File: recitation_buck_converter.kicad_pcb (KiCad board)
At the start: 2 copper layers, 25.4 x 25.4 mm, 11 parts, among them J1 VIN, J2 Conn_01x02_MountingPin, U1 TPS54233

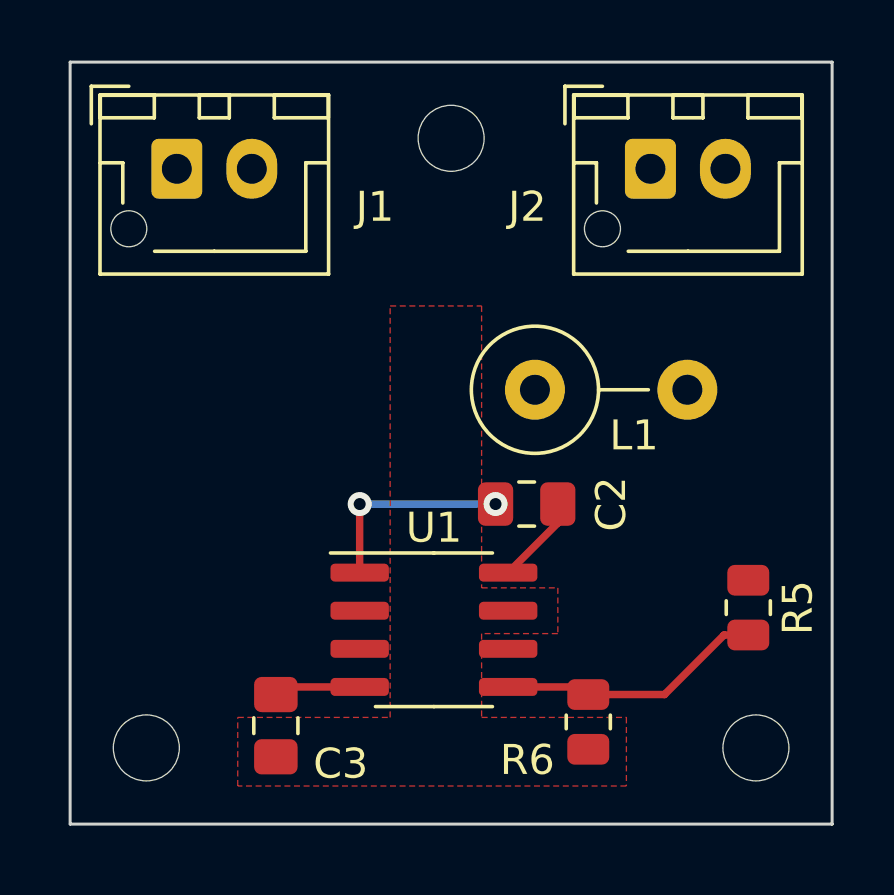
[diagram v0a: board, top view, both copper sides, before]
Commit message: feat: add output components, float EN, and layouu with good track width
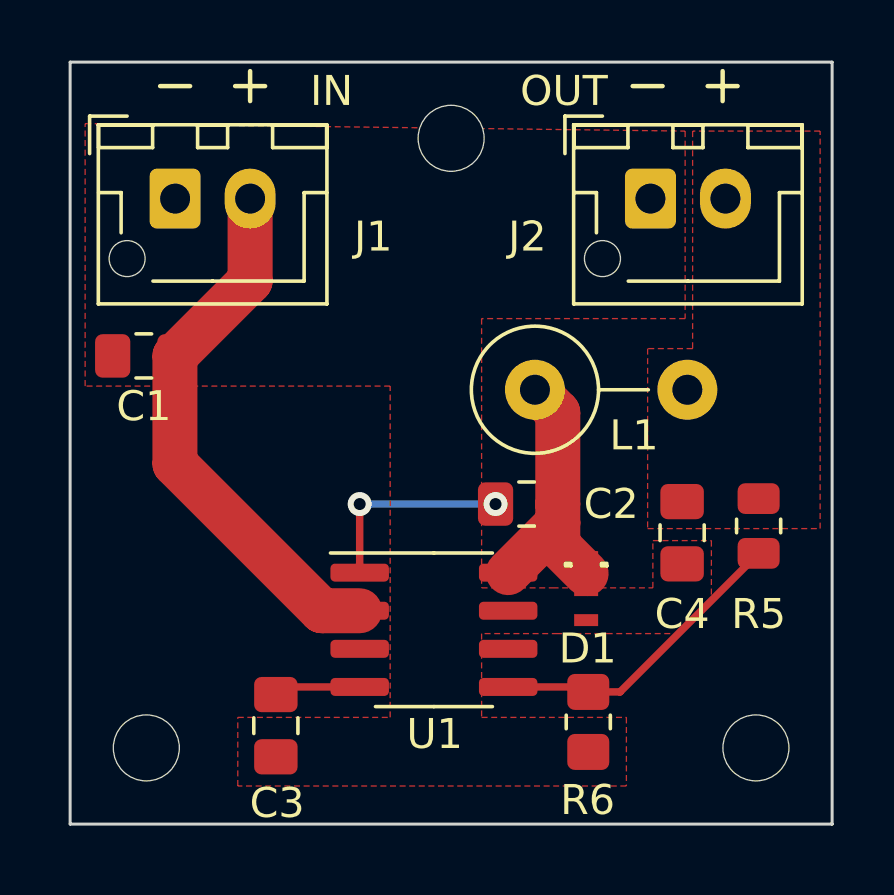
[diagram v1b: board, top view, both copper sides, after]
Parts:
- added C1: 10u, Capacitor_SMD:C_0805_2012Metric_Pad1.18x1.45mm_HandSolder, F.Cu at (129.5, 86.0)
- added C4: 1.5u, Capacitor_SMD:C_0805_2012Metric_Pad1.18x1.45mm_HandSolder, F.Cu at (147.4, 91.9)
- added D1: D_Schottky, ToshibaUS2H:US2H, F.Cu at (144.2, 94.0)
- J1: value VIN -> Conn_01x02_MountingPin
- R6: footprint Resistor_SMD:R_0805_2012Metric -> Resistor_SMD:R_0805_2012Metric_Pad1.20x1.40mm_HandSolder
- moved R5 2.74 mm to (149.9, 91.7)
- moved J1 1.00 mm to (130.5, 80.8)
- moved J2 0.99 mm to (146.3, 80.8)
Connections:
- U1 pad 3: VIN -> unconnected-(U1-EN-Pad3)
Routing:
- net VIN: track 0.00 -> 18.1 mm
- net Net-(D1-K): track 2.97 -> 9.17 mm
- net /Feedback/Vsense: track 8.93 -> 10.4 mm
- added copper zone on F.Cu, net VOUT
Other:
- board text added: "IN"
- board text added: "OUT"

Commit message: feat: add compensation network; finish pcb
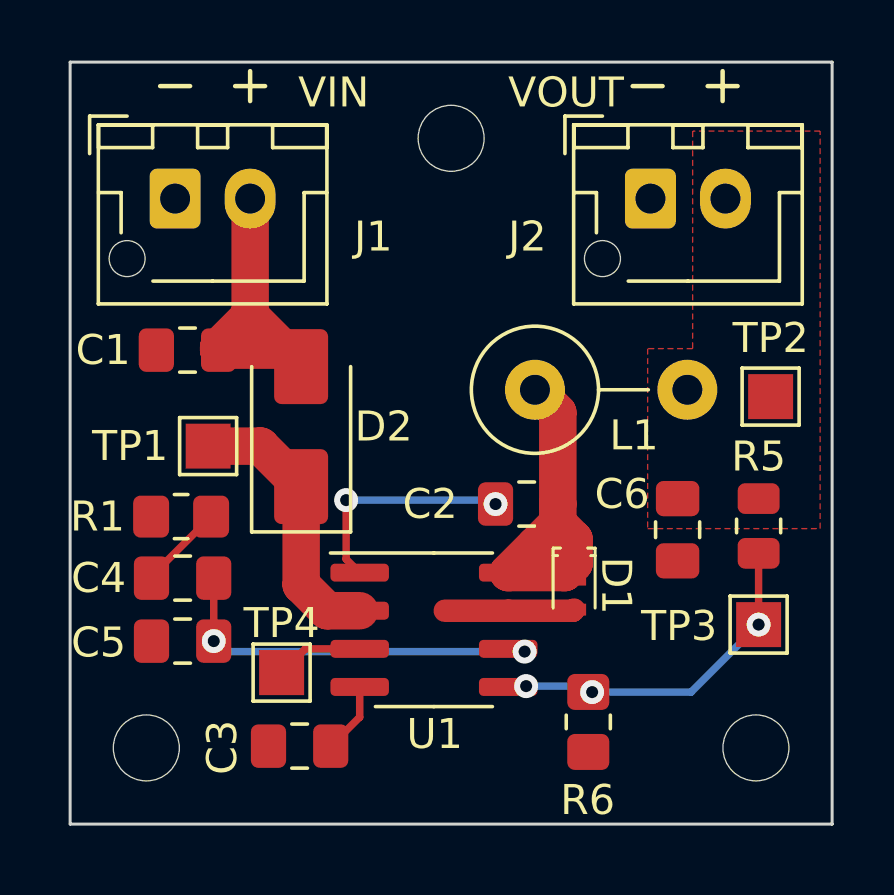
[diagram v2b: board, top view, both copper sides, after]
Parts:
- added C5: 240p, Capacitor_SMD:C_0805_2012Metric_Pad1.18x1.45mm_HandSolder, F.Cu at (130.8, 95.5)
- added C6: 1.5u, Capacitor_SMD:C_0805_2012Metric_Pad1.18x1.45mm_HandSolder, F.Cu at (147.2, 91.8)
- added D2: D, Diode_SMD:D_SMA, F.Cu at (134.7, 88.3)
- added R1: 5.23k, Resistor_SMD:R_0805_2012Metric_Pad1.20x1.40mm_HandSolder, F.Cu at (130.7, 91.3)
- added TP1: TPVin, TestPoint:TestPoint_Pad_1.5x1.5mm, F.Cu at (131.6, 89.0)
- added TP2: TPVout, TestPoint:TestPoint_Pad_1.5x1.5mm, F.Cu at (150.3, 87.3)
- added TP3: TPVsense, TestPoint:TestPoint_Pad_1.5x1.5mm, F.Cu at (149.9, 95.0)
- added TP4: TPEN, TestPoint:TestPoint_Pad_1.5x1.5mm, F.Cu at (134.1, 96.5)
- C4: value 1.5u -> 820p
- J1, J2: value Conn_01x02_MountingPin -> Conn_01x02_Pin
- moved C4 16.7 mm to (130.8, 93.4), turned to 180 degrees
- moved C1 1.47 mm to (130.9, 85.8)
- moved C3 1.04 mm to (134.7, 99.0), turned to 180 degrees
- moved D1 0.53 mm to (143.8, 93.7)
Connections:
- net Net-(D1-K) renamed PHPin
- C4 pad 1: VOUT -> Net-(U1-COMP)
- C4 pad 2: GND -> Net-(C4-Pad2)
- U1 pad 2: VIN -> Net-(D2-K)
- U1 pad 3: unconnected-(U1-EN-Pad3) -> TPS5_EN
- U1 pad 6: unconnected-(U1-COMP-Pad6) -> Net-(U1-COMP)
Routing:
- net Net-(U1-COMP): track 0.00 -> 13.2 mm, vias 0 -> 2
- net Net-(D2-K): track 0.00 -> 9.24 mm
- net VIN: track 18.1 -> 10.9 mm
- net GND: track 0.00 -> 4.33 mm
- net PHPin: track 9.17 -> 12.5 mm
- net TPS5_EN: track 0.00 -> 2.93 mm
- net Net-(C4-Pad2): track 0.00 -> 2.87 mm
- net /Feedback/Vsense: track 10.4 -> 11.9 mm, vias 0 -> 3
- net Net-(U1-BOOT): track 6.82 -> 7.64 mm
- net Net-(U1-SS): track 2.90 -> 2.37 mm
- added copper zone on B.Cu, net GND
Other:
- board text added: "VIN"
- board text added: "VOUT"
- board text removed: "IN"
- board text removed: "OUT"

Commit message: fix(pcb): move dimensions to drawing layer
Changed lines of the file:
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@@
       (outputformat 1)
       (mirror false)
-      (drillshape 1)
+      (drillshape 0)
       (scaleselection 1)
-      (outputdirectory "")
+      (outputdirectory "plot_gerbers/")
     )
   )
@@
     (fp_line (start 1 0.625) (end -1 0.625)
       (stroke (width 0.1) (type solid)) (layer "F.Fab"))
-    (pad "1" smd roundrect (at -1 0 180) (size 1.2 1.4) (layers "F.Cu" "F.Paste" "F.Mask") (roundrect_rratio 0.208333)
+    (pad "1" smd roundrect (at -1 0 180) (size 1.2 1.4) (layers "F.Cu" "F.Paste" "F.Mask") (roundrect_rratio 0.2083333333)
       (net 9 "Net-(C4-Pad2)") (pintype "passive"))
-    (pad "2" smd roundrect (at 1 0 180) (size 1.2 1.4) (layers "F.Cu" "F.Paste" "F.Mask") (roundrect_rratio 0.208333)
+    (pad "2" smd roundrect (at 1 0 180) (size 1.2 1.4) (layers "F.Cu" "F.Paste" "F.Mask") (roundrect_rratio 0.2083333333)
       (net 3 "GND") (pintype "passive"))
     (model "${KICAD6_3DMODEL_DIR}/Resistor_SMD.3dshapes/R_0805_2012Metric.wrl"
@@
     (fp_line (start 1 0.625) (end -1 0.625)
       (stroke (width 0.1) (type solid)) (layer "F.Fab"))
-    (pad "1" smd roundrect (at -1.0375 0 180) (size 1.175 1.45) (layers "F.Cu" "F.Paste" "F.Mask") (roundrect_rratio 0.212766)
+    (pad "1" smd roundrect (at -1.0375 0 180) (size 1.175 1.45) (layers "F.Cu" "F.Paste" "F.Mask") (roundrect_rratio 0.2127659574)
       (net 2 "Net-(U1-SS)") (pintype "passive"))
-    (pad "2" smd roundrect (at 1.0375 0 180) (size 1.175 1.45) (layers "F.Cu" "F.Paste" "F.Mask") (roundrect_rratio 0.212766)
+    (pad "2" smd roundrect (at 1.0375 0 180) (size 1.175 1.45) (layers "F.Cu" "F.Paste" "F.Mask") (roundrect_rratio 0.2127659574)
       (net 3 "GND") (pintype "passive"))
     (model "${KICAD6_3DMODEL_DIR}/Capacitor_SMD.3dshapes/C_0805_2012Metric.wrl"
@@
     (fp_line (start 1 0.625) (end -1 0.625)
       (stroke (width 0.1) (type solid)) (layer "F.Fab"))
-    (pad "1" smd roundrect (at -1.0375 0 180) (size 1.175 1.45) (layers "F.Cu" "F.Paste" "F.Mask") (roundrect_rratio 0.212766)
+    (pad "1" smd roundrect (at -1.0375 0 180) (size 1.175 1.45) (layers "F.Cu" "F.Paste" "F.Mask") (roundrect_rratio 0.2127659574)
       (net 4 "VIN") (pintype "passive"))
-    (pad "2" smd roundrect (at 1.0375 0 180) (size 1.175 1.45) (layers "F.Cu" "F.Paste" "F.Mask") (roundrect_rratio 0.212766)
+    (pad "2" smd roundrect (at 1.0375 0 180) (size 1.175 1.45) (layers "F.Cu" "F.Paste" "F.Mask") (roundrect_rratio 0.2127659574)
       (net 3 "GND") (pintype "passive"))
     (model "${KICAD6_3DMODEL_DIR}/Capacitor_SMD.3dshapes/C_0805_2012Metric.wrl"
@@
       (stroke (width 0.1) (type solid)) (layer "F.Fab"))
     (pad "" np_thru_hole circle (at -1.6 2) (size 1.2 1.2) (drill 1.2) (layers "*.Cu" "*.Mask"))
-    (pad "1" thru_hole roundrect (at 0 0) (size 1.7 2) (drill 1) (layers "*.Cu" "*.Mask") (roundrect_rratio 0.147059)
+    (pad "1" thru_hole roundrect (at 0 0) (size 1.7 2) (drill 1) (layers "*.Cu" "*.Mask") (roundrect_rratio 0.1470588235)
       (net 3 "GND") (pinfunction "Pin_1") (pintype "passive"))
     (pad "2" thru_hole oval (at 2.5 0) (size 1.7 2) (drill 1) (layers "*.Cu" "*.Mask")
@@
     (fp_line (start 1 0.625) (end -1 0.625)
       (stroke (width 0.1) (type solid)) (layer "F.Fab"))
-    (pad "1" smd roundrect (at -1.0375 0 270) (size 1.175 1.45) (layers "F.Cu" "F.Paste" "F.Mask") (roundrect_rratio 0.212766)
+    (pad "1" smd roundrect (at -1.0375 0 270) (size 1.175 1.45) (layers "F.Cu" "F.Paste" "F.Mask") (roundrect_rratio 0.2127659574)
       (net 5 "VOUT") (pintype "passive"))
-    (pad "2" smd roundrect (at 1.0375 0 270) (size 1.175 1.45) (layers "F.Cu" "F.Paste" "F.Mask") (roundrect_rratio 0.212766)
+    (pad "2" smd roundrect (at 1.0375 0 270) (size 1.175 1.45) (layers "F.Cu" "F.Paste" "F.Mask") (roundrect_rratio 0.2127659574)
       (net 3 "GND") (pintype "passive"))
     (model "${KICAD6_3DMODEL_DIR}/Capacitor_SMD.3dshapes/C_0805_2012Metric.wrl"
@@
     (fp_line (start 1 0.625) (end -1 0.625)
       (stroke (width 0.1) (type solid)) (layer "F.Fab"))
-    (pad "1" smd roundrect (at -1.0375 0) (size 1.175 1.45) (layers "F.Cu" "F.Paste" "F.Mask") (roundrect_rratio 0.212766)
+    (pad "1" smd roundrect (at -1.0375 0) (size 1.175 1.45) (layers "F.Cu" "F.Paste" "F.Mask") (roundrect_rratio 0.2127659574)
       (net 1 "Net-(U1-BOOT)") (pintype "passive"))
-    (pad "2" smd roundrect (at 1.0375 0) (size 1.175 1.45) (layers "F.Cu" "F.Paste" "F.Mask") (roundrect_rratio 0.212766)
+    (pad "2" smd roundrect (at 1.0375 0) (size 1.175 1.45) (layers "F.Cu" "F.Paste" "F.Mask") (roundrect_rratio 0.2127659574)
       (net 11 "PHPin") (pintype "passive"))
     (model "${KICAD6_3DMODEL_DIR}/Capacitor_SMD.3dshapes/C_0805_2012Metric.wrl"
@@
       (stroke (width 0.1) (type solid)) (layer "F.Fab"))
     (pad "" np_thru_hole circle (at -1.6 2) (size 1.2 1.2) (drill 1.2) (layers "*.Cu" "*.Mask"))
-    (pad "1" thru_hole roundrect (at 0 0) (size 1.7 2) (drill 1) (layers "*.Cu" "*.Mask") (roundrect_rratio 0.147059)
+    (pad "1" thru_hole roundrect (at 0 0) (size 1.7 2) (drill 1) (layers "*.Cu" "*.Mask") (roundrect_rratio 0.1470588235)
       (net 3 "GND") (pinfunction "Pin_1") (pintype "passive"))
     (pad "2" thru_hole oval (at 2.5 0) (size 1.7 2) (drill 1) (layers "*.Cu" "*.Mask")
@@
     (fp_line (start 1 0.625) (end -1 0.625)
       (stroke (width 0.1) (type solid)) (layer "F.Fab"))
-    (pad "1" smd roundrect (at -1.0375 0 180) (size 1.175 1.45) (layers "F.Cu" "F.Paste" "F.Mask") (roundrect_rratio 0.212766)
+    (pad "1" smd roundrect (at -1.0375 0 180) (size 1.175 1.45) (layers "F.Cu" "F.Paste" "F.Mask") (roundrect_rratio 0.2127659574)
       (net 7 "Net-(U1-COMP)") (pintype "passive"))
-    (pad "2" smd roundrect (at 1.0375 0 180) (size 1.175 1.45) (layers "F.Cu" "F.Paste" "F.Mask") (roundrect_rratio 0.212766)
+    (pad "2" smd roundrect (at 1.0375 0 180) (size 1.175 1.45) (layers "F.Cu" "F.Paste" "F.Mask") (roundrect_rratio 0.2127659574)
       (net 3 "GND") (pintype "passive"))
     (model "${KICAD6_3DMODEL_DIR}/Capacitor_SMD.3dshapes/C_0805_2012Metric.wrl"
@@
     (fp_line (start 1 0.625) (end -1 0.625)
       (stroke (width 0.1) (type solid)) (layer "F.Fab"))
-    (pad "1" smd roundrect (at -0.9125 0 270) (size 1.025 1.4) (layers "F.Cu" "F.Paste" "F.Mask") (roundrect_rratio 0.243902)
+    (pad "1" smd roundrect (at -0.9125 0 270) (size 1.025 1.4) (layers "F.Cu" "F.Paste" "F.Mask") (roundrect_rratio 0.243902439)
       (net 5 "VOUT") (pintype "passive"))
-    (pad "2" smd roundrect (at 0.9125 0 270) (size 1.025 1.4) (layers "F.Cu" "F.Paste" "F.Mask") (roundrect_rratio 0.243902)
+    (pad "2" smd roundrect (at 0.9125 0 270) (size 1.025 1.4) (layers "F.Cu" "F.Paste" "F.Mask") (roundrect_rratio 0.243902439)
       (net 6 "/Feedback{slash}Vsense") (pintype "passive"))
     (model "${KICAD6_3DMODEL_DIR}/Resistor_SMD.3dshapes/R_0805_2012Metric.wrl"
@@
     (fp_line (start 1 0.625) (end -1 0.625)
       (stroke (width 0.1) (type solid)) (layer "F.Fab"))
-    (pad "1" smd roundrect (at -1.0375 0 180) (size 1.175 1.45) (layers "F.Cu" "F.Paste" "F.Mask") (roundrect_rratio 0.212766)
+    (pad "1" smd roundrect (at -1.0375 0 180) (size 1.175 1.45) (layers "F.Cu" "F.Paste" "F.Mask") (roundrect_rratio 0.2127659574)
       (net 7 "Net-(U1-COMP)") (pintype "passive"))
-    (pad "2" smd roundrect (at 1.0375 0 180) (size 1.175 1.45) (layers "F.Cu" "F.Paste" "F.Mask") (roundrect_rratio 0.212766)
+    (pad "2" smd roundrect (at 1.0375 0 180) (size 1.175 1.45) (layers "F.Cu" "F.Paste" "F.Mask") (roundrect_rratio 0.2127659574)
       (net 9 "Net-(C4-Pad2)") (pintype "passive"))
     (model "${KICAD6_3DMODEL_DIR}/Capacitor_SMD.3dshapes/C_0805_2012Metric.wrl"
@@
     (fp_line (start 1 0.625) (end -1 0.625)
       (stroke (width 0.1) (type solid)) (layer "F.Fab"))
-    (pad "1" smd roundrect (at -1 0 270) (size 1.2 1.4) (layers "F.Cu" "F.Paste" "F.Mask") (roundrect_rratio 0.208333)
+    (pad "1" smd roundrect (at -1 0 270) (size 1.2 1.4) (layers "F.Cu" "F.Paste" "F.Mask") (roundrect_rratio 0.2083333333)
       (net 6 "/Feedback{slash}Vsense") (pintype "passive"))
-    (pad "2" smd roundrect (at 1 0 270) (size 1.2 1.4) (layers "F.Cu" "F.Paste" "F.Mask") (roundrect_rratio 0.208333)
+    (pad "2" smd roundrect (at 1 0 270) (size 1.2 1.4) (layers "F.Cu" "F.Paste" "F.Mask") (roundrect_rratio 0.2083333333)
       (net 3 "GND") (pintype "passive"))
     (model "${KICAD6_3DMODEL_DIR}/Resistor_SMD.3dshapes/R_0805_2012Metric.wrl"
@@
     (effects (font (size 1 1) (thickness 0.15)) (justify left bottom))
   )
-  (dimension (type aligned) (layer "F.Cu")
+  (dimension (type aligned) (layer "Dwgs.User")
     (pts (xy 127 76.2) (xy 127 101.6))
     (height 4.999999)
-    (gr_text "25.4000 mm" (at 120.200001 88.9 90) (layer "F.Cu")
+    (gr_text "25.4000 mm" (at 120.200001 88.9 90) (layer "Dwgs.User")
       (effects (font (size 1.5 1.5) (thickness 0.3)))
     )
@@
     (style (thickness 0.2) (arrow_length 1.27) (text_position_mode 0) (extension_height 0.58642) (extension_offset 0.5) keep_text_aligned)
   )
-  (dimension (type aligned) (layer "F.Cu")
+  (dimension (type aligned) (layer "Dwgs.User")
     (pts (xy 127 76.2) (xy 152.4 76.2))
     (height -4.45)
-    (gr_text "25.4000 mm" (at 139.7 69.95) (layer "F.Cu")
+    (gr_text "25.4000 mm" (at 139.7 69.95) (layer "Dwgs.User")
       (effects (font (size 1.5 1.5) (thickness 0.3)))
     )

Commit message: feat: add vias for front-back ground fill
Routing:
- net GND: vias 0 -> 45
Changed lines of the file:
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@@
   (segment (start 143.762 94.488) (end 143.8 94.45) (width 0.75) (layer "F.Cu") (net 3))
   (segment (start 141.602 94.488) (end 139.488 94.488) (width 0.75) (layer "F.Cu") (net 3))
+  (via (at 147 98.5) (size 0.8) (drill 0.4) (layers "F.Cu" "B.Cu") (free) (net 3))
+  (via (at 138.5 85) (size 0.8) (drill 0.4) (layers "F.Cu" "B.Cu") (free) (net 3))
+  (via (at 147 100.5) (size 0.8) (drill 0.4) (layers "F.Cu" "B.Cu") (free) (net 3))
+  (via (at 151.5 93.5) (size 0.8) (drill 0.4) (layers "F.Cu" "B.Cu") (free) (net 3))
+  (via (at 138.5 87) (size 0.8) (drill 0.4) (layers "F.Cu" "B.Cu") (free) (net 3))
+  (via (at 147 96) (size 0.8) (drill 0.4) (layers "F.Cu" "B.Cu") (free) (net 3))
+  (via (at 132 97) (size 0.8) (drill 0.4) (layers "F.Cu" "B.Cu") (free) (net 3))
+  (via (at 132 100.5) (size 0.8) (drill 0.4) (layers "F.Cu" "B.Cu") (free) (net 3))
+  (via (at 138.5 93) (size 0.8) (drill 0.4) (layers "F.Cu" "B.Cu") (free) (net 3))
+  (via (at 128 92.5) (size 0.8) (drill 0.4) (layers "F.Cu" "B.Cu") (free) (net 3))
+  (via (at 138.5 94) (size 0.8) (drill 0.4) (layers "F.Cu" "B.Cu") (free) (net 3))
+  (via (at 145.5 89.5) (size 0.8) (drill 0.4) (layers "F.Cu" "B.Cu") (free) (net 3))
+  (via (at 129 87.5) (size 0.8) (drill 0.4) (layers "F.Cu" "B.Cu") (free) (net 3))
+  (via (at 151.5 92.5) (size 0.8) (drill 0.4) (layers "F.Cu" "B.Cu") (free) (net 3))
+  (via (at 137.5 85) (size 0.8) (drill 0.4) (layers "F.Cu" "B.Cu") (free) (net 3))
+  (via (at 137.5 86) (size 0.8) (drill 0.4) (layers "F.Cu" "B.Cu") (free) (net 3))
+  (via (at 133 93.5) (size 0.8) (drill 0.4) (layers "F.Cu" "B.Cu") (free) (net 3))
+  (via (at 139.5 86) (size 0.8) (drill 0.4) (layers "F.Cu" "B.Cu") (free) (net 3))
+  (via (at 134.5 84) (size 0.8) (drill 0.4) (layers "F.Cu" "B.Cu") (free) (net 3))
+  (via (at 137.5 87) (size 0.8) (drill 0.4) (layers "F.Cu" "B.Cu") (free) (net 3))
+  (via (at 142.5 98) (size 0.8) (drill 0.4) (layers "F.Cu" "B.Cu") (free) (net 3))
+  (via (at 138.5 97) (size 0.8) (drill 0.4) (layers "F.Cu" "B.Cu") (free) (net 3))
+  (via (at 139.5 92) (size 0.8) (drill 0.4) (layers "F.Cu" "B.Cu") (free) (net 3))
+  (via (at 139.5 89.5) (size 0.8) (drill 0.4) (layers "F.Cu" "B.Cu") (free) (net 3))
+  (via (at 138.5 95) (size 0.8) (drill 0.4) (layers "F.Cu" "B.Cu") (free) (net 3))
+  (via (at 144.5 89.5) (size 0.8) (drill 0.4) (layers "F.Cu" "B.Cu") (free) (net 3))
+  (via (at 139.5 85) (size 0.8) (drill 0.4) (layers "F.Cu" "B.Cu") (free) (net 3))
+  (via (at 151.5 95.5) (size 0.8) (drill 0.4) (layers "F.Cu" "B.Cu") (free) (net 3))
+  (via (at 137.5 92) (size 0.8) (drill 0.4) (layers "F.Cu" "B.Cu") (free) (net 3))
+  (via (at 130 87.5) (size 0.8) (drill 0.4) (layers "F.Cu" "B.Cu") (free) (net 3))
+  (via (at 138.5 89.5) (size 0.8) (drill 0.4) (layers "F.Cu" "B.Cu") (free) (net 3))
+  (via (at 151.5 96.5) (size 0.8) (drill 0.4) (layers "F.Cu" "B.Cu") (free) (net 3))
+  (via (at 139.5 87) (size 0.8) (drill 0.4) (layers "F.Cu" "B.Cu") (free) (net 3))
+  (via (at 151.5 94.5) (size 0.8) (drill 0.4) (layers "F.Cu" "B.Cu") (free) (net 3))
+  (via (at 137.5 89.5) (size 0.8) (drill 0.4) (layers "F.Cu" "B.Cu") (free) (net 3))
+  (via (at 139.5 93) (size 0.8) (drill 0.4) (layers "F.Cu" "B.Cu") (free) (net 3))
+  (via (at 138.5 86) (size 0.8) (drill 0.4) (layers "F.Cu" "B.Cu") (free) (net 3))
+  (via (at 128 94.5) (size 0.8) (drill 0.4) (layers "F.Cu" "B.Cu") (free) (net 3))
+  (via (at 138.5 92) (size 0.8) (drill 0.4) (layers "F.Cu" "B.Cu") (free) (net 3))
+  (via (at 133 92.5) (size 0.8) (drill 0.4) (layers "F.Cu" "B.Cu") (free) (net 3))
+  (via (at 146 96) (size 0.8) (drill 0.4) (layers "F.Cu" "B.Cu") (free) (net 3))
+  (via (at 139.5 97) (size 0.8) (drill 0.4) (layers "F.Cu" "B.Cu") (free) (net 3))
+  (via (at 128 96.5) (size 0.8) (drill 0.4) (layers "F.Cu" "B.Cu") (free) (net 3))
+  (via (at 128 87.5) (size 0.8) (drill 0.4) (layers "F.Cu" "B.Cu") (free) (net 3))
+  (via (at 131.5 84) (size 0.8) (drill 0.4) (layers "F.Cu" "B.Cu") (free) (net 3))
   (segment (start 131.95 85.8) (end 131.95 85.7) (width 1.25) (layer "F.Cu") (net 4))
   (segment (start 131.95 85.7) (end 133 84.65) (width 1.25) (layer "F.Cu") (net 4))
